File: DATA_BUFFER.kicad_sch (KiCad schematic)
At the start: 9 parts, among them IC301 ${DEVICE}

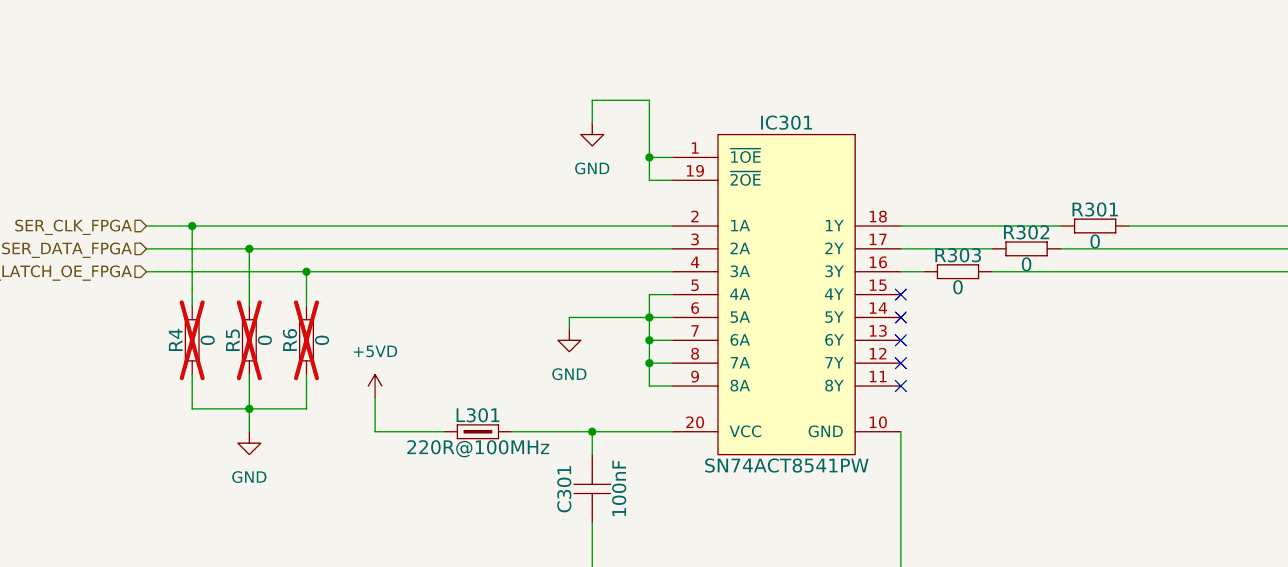
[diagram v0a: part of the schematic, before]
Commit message: Rerouted PCB Logic part
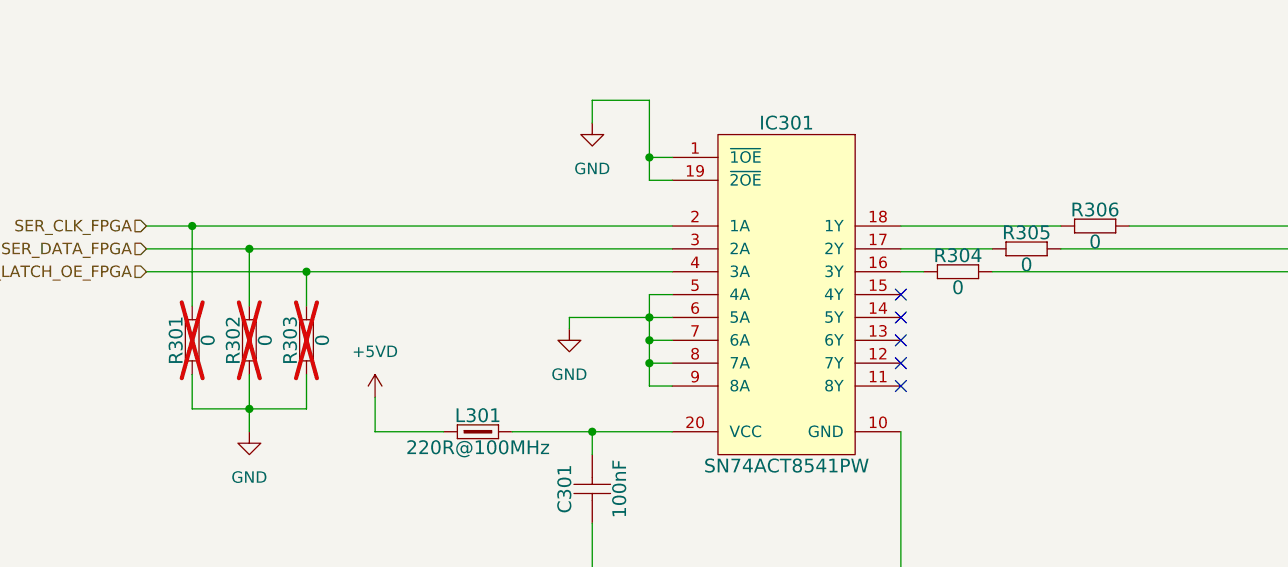
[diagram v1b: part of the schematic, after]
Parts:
- renumbered R4 to R301, R5 to R302, R6 to R303, R303 to R304, R302 to R305, R301 to R306
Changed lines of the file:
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@@
 		(dnp no)
 		(fields_autoplaced yes)
-		(property "Reference" "#PWR0304"
+		(property "Reference" "#PWR0305"
 			(at 114.3 118.11 0)
 			(effects
@@
 			(project "8CH_Analog_Front_END"
 				(path "/41597329-5145-432a-9041-5bc2cec82d9b/00694170-70ef-4ff0-8ee8-0493ce41d04f"
-					(reference "#PWR0304")
+					(reference "#PWR0305")
 					(unit 1)
 				)
@@
 		(dnp no)
 		(fields_autoplaced yes)
-		(property "Reference" "#PWR0303"
+		(property "Reference" "#PWR0302"
 			(at 90.17 92.71 0)
 			(effects
@@
 			(project "8CH_Analog_Front_END"
 				(path "/41597329-5145-432a-9041-5bc2cec82d9b/00694170-70ef-4ff0-8ee8-0493ce41d04f"
-					(reference "#PWR0303")
+					(reference "#PWR0302")
 					(unit 1)
 				)
@@
 		(on_board yes)
 		(dnp no)
-		(property "Reference" "R302"
+		(property "Reference" "R305"
 			(at 162.56 70.612 0)
 			(effects
@@
 			(project "8CH_Analog_Front_END"
 				(path "/41597329-5145-432a-9041-5bc2cec82d9b/00694170-70ef-4ff0-8ee8-0493ce41d04f"
-					(reference "R302")
+					(reference "R305")
 					(unit 1)
 				)
@@
 		(dnp no)
 		(fields_autoplaced yes)
-		(property "Reference" "#PWR0302"
+		(property "Reference" "#PWR0303"
 			(at 111.76 87.63 0)
 			(effects
@@
 			(project "8CH_Analog_Front_END"
 				(path "/41597329-5145-432a-9041-5bc2cec82d9b/00694170-70ef-4ff0-8ee8-0493ce41d04f"
-					(reference "#PWR0302")
+					(reference "#PWR0303")
 					(unit 1)
 				)
@@
 		(dnp no)
 		(fields_autoplaced yes)
-		(property "Reference" "#PWR0301"
+		(property "Reference" "#PWR0304"
 			(at 114.3 64.77 0)
 			(effects
@@
 			(project "8CH_Analog_Front_END"
 				(path "/41597329-5145-432a-9041-5bc2cec82d9b/00694170-70ef-4ff0-8ee8-0493ce41d04f"
-					(reference "#PWR0301")
+					(reference "#PWR0304")
 					(unit 1)
 				)
@@
 		(on_board yes)
 		(dnp no)
-		(property "Reference" "R303"
+		(property "Reference" "R304"
 			(at 154.94 73.152 0)
 			(effects
@@
 			(project "8CH_Analog_Front_END"
 				(path "/41597329-5145-432a-9041-5bc2cec82d9b/00694170-70ef-4ff0-8ee8-0493ce41d04f"
-					(reference "R303")
+					(reference "R304")
 					(unit 1)
 				)
@@
 		(on_board yes)
 		(dnp yes)
-		(property "Reference" "R4"
+		(property "Reference" "R301"
 			(at 68.072 82.55 0)
 			(effects
@@
 			(project "8CH_Analog_Front_END"
 				(path "/41597329-5145-432a-9041-5bc2cec82d9b/00694170-70ef-4ff0-8ee8-0493ce41d04f"
-					(reference "R4")
+					(reference "R301")
 					(unit 1)
 				)
@@
 		(on_board yes)
 		(dnp yes)
-		(property "Reference" "R6"
+		(property "Reference" "R303"
 			(at 80.772 82.55 0)
 			(effects
@@
 			(project "8CH_Analog_Front_END"
 				(path "/41597329-5145-432a-9041-5bc2cec82d9b/00694170-70ef-4ff0-8ee8-0493ce41d04f"
-					(reference "R6")
+					(reference "R303")
 					(unit 1)
 				)
@@
 		(dnp no)
 		(fields_autoplaced yes)
-		(property "Reference" "#PWR06"
+		(property "Reference" "#PWR0301"
 			(at 76.2 99.06 0)
 			(effects
@@
 			(project "8CH_Analog_Front_END"
 				(path "/41597329-5145-432a-9041-5bc2cec82d9b/00694170-70ef-4ff0-8ee8-0493ce41d04f"
-					(reference "#PWR06")
+					(reference "#PWR0301")
 					(unit 1)
 				)
@@
 		(on_board yes)
 		(dnp no)
-		(property "Reference" "R301"
+		(property "Reference" "R306"
 			(at 170.18 68.072 0)
 			(effects
@@
 			(project "8CH_Analog_Front_END"
 				(path "/41597329-5145-432a-9041-5bc2cec82d9b/00694170-70ef-4ff0-8ee8-0493ce41d04f"
-					(reference "R301")
+					(reference "R306")
 					(unit 1)
 				)
@@
 		(on_board yes)
 		(dnp yes)
-		(property "Reference" "R5"
+		(property "Reference" "R302"
 			(at 74.422 82.55 0)
 			(effects
@@
 			(project "8CH_Analog_Front_END"
 				(path "/41597329-5145-432a-9041-5bc2cec82d9b/00694170-70ef-4ff0-8ee8-0493ce41d04f"
-					(reference "R5")
+					(reference "R302")
 					(unit 1)
 				)
@@
 		(dnp no)
 		(fields_autoplaced yes)
-		(property "Reference" "#PWR0305"
+		(property "Reference" "#PWR0306"
 			(at 148.59 118.11 0)
 			(effects
@@
 			(project "8CH_Analog_Front_END"
 				(path "/41597329-5145-432a-9041-5bc2cec82d9b/00694170-70ef-4ff0-8ee8-0493ce41d04f"
-					(reference "#PWR0305")
+					(reference "#PWR0306")
 					(unit 1)
 				)

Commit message: WIP snapshot
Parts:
- removed IC301: ${DEVICE}, ICs And Semiconductors SMD:SOP65P640X120-20N, symbol CERN:Standard Logic/SN74ACT8541PW
- removed L301: 220R@100MHz, Inductors SMD:INDC1608X95N, symbol CERN:Inductors SMD/IND0603_MURATA_BLM18SG221TN1 [alt]
- removed R301, R302, R303, R304, R305, R306: 0, Resistors SMD:RESC1005X40N, symbol CERN:Resistors SMD/R0402_0R_JUMPER
- added C301, C302, C304: 100nF, Capacitors SMD:CAPC1005X55N, symbol CERN:Capacitors SMD/CC0402_100NF_25V_10%_X7R_YUDEN_TMK105B7104KVHF
- added IC301, IC302: ${DEVICE}, ICs And Semiconductors SMD:TEXAS_RHL (S-PVQFN-N24), symbol CERN_Linux:Standard Logic/SN74LVC8T245RHL
- added R301, R302, R303, R304, R306, R307, R309, R310, R311, R312, R313, R314, R315, R316, R317, R318, R319, R320, R321, R322, R323, R324, R325, R326, R327, R328: 22R6, Resistors SMD:RESC1005X40N, symbol CERN:Resistors SMD/R0402_22R6_1%_0.063W_100PPM
- added R305, R308: 220, Resistors SMD:RESC1005X40N, symbol CERN:Resistors SMD/R0402_220R_1%_0.0625W_100PPM
- renumbered C301 to C303
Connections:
- net GND: now also C301.1, C302.1, C304.1, IC301.11 (GND), IC301.12 (GND), IC301.13 (GND), IC301.22 (~{OE}), IC302.11 (GND), IC302.12 (GND), IC302.13 (GND), IC302.22 (~{OE}), R305.1, R308.1
- net SER_CLK_FPGA: now also R302.1
- net +3V3D: now reaches C303.2
- net +3V3D: now also C301.2, C302.2, C304.2, IC301.1 (VCCA), IC301.2 (DIR), IC301.23 (VCCB), IC301.24 (VCCB), IC302.1 (VCCA), IC302.2 (DIR), IC302.23 (VCCB), IC302.24 (VCCB)
- new net: IC302.10 (A8), IC302.7 (A5), IC302.8 (A6), IC302.9 (A7), R302.2, R305.2
- new net: IC301.9 (A7), R307.2
- new net: IC301.8 (A6), R311.2
- new net: IC301.3 (A1), R303.2
- new net: IC301.20 (B2), R313.1
- new net: IC301.21 (B1), R321.1
- new net: IC302.21 (B1), R325.1
- new net: IC301.14 (B8), R316.1
- new net: IC302.3 (A1), IC302.4 (A2), IC302.5 (A3), IC302.6 (A4), R301.2, R308.2
- new net: IC301.17 (B5), R323.1
- new net: IC302.16 (B6), R319.1
- new net: IC301.5 (A3), R306.2
- new net: IC301.18 (B4), R314.1
- new net: IC302.14 (B8), R320.1
- new net: IC302.15 (B7), R328.1
- new net: IC302.17 (B5), R327.1
- new net: IC302.18 (B4), R318.1
- new net: IC302.19 (B3), R326.1
- new net: IC302.20 (B2), R317.1
- new net: IC301.10 (A8), R312.2
- new net: IC301.6 (A4), R310.2
- new net: IC301.19 (B3), R322.1
- new net: IC301.4 (A2), R309.2
- new net: IC301.15 (B7), R324.1
- new net: IC301.16 (B6), R315.1
- new net: IC301.7 (A5), R304.2
- new net SER_CLK_CH0: R327.2
- new net SER_CLK_CH1: R319.2
- new net SER_CLK_CH2: R328.2
- new net SER_CLK_CH3: R320.2
- new net SER_DATA0: R321.2
- new net SER_DATA1: R313.2
- new net SER_DATA2: R322.2
- new net SER_DATA3: R314.2
- new net SER_DATA4: R323.2
- new net SER_DATA5: R315.2
- new net SER_DATA6: R324.2
- new net SER_DATA7: R316.2
- new net SER_DATA_FPGA0: R303.1
- new net SER_DATA_FPGA1: R309.1
- new net SER_DATA_FPGA2: R306.1
- new net SER_DATA_FPGA3: R310.1
- new net SER_DATA_FPGA4: R304.1
- new net SER_DATA_FPGA5: R311.1
- new net SER_DATA_FPGA6: R307.1
- new net SER_DATA_FPGA7: R312.1
- new net SER_RCLK_CH0: R325.2
- new net SER_RCLK_CH1: R317.2
- new net SER_RCLK_CH2: R326.2
- new net SER_RCLK_CH3: R318.2
- new net SER_RCLK_FPGA: R301.1
- no-connect marks 5 -> 0
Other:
- note added: "Place series resistors close to IC6."
- note added: "Place series resistors close to KR SoM connector."
- note added: "Shiftreg DATA buffer. - DIR=1 (A->B), powered from Vcca (3.3V) - Each SER_DATA line handles a chain of 3x8-bit SRs (24-bits in total) - The above gives 16ns x 24 = 500ns update time (62.5 MHz CLK, abort gap is 3us) - Two SER_DATA lines go to a single AFE block (one for channel A, one for channel B)"
- note added: "Shiftreg clocks buffer. - DIR=1 (A->B), powered from Vcca (3.3V) - Acts as a clock fanout to avoid excessive load on the clock lines (1 dedicated shiftreg clock per plane)."
- note removed: "DATA"
- moved on the sheet: C303

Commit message: Update project files and backups
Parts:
- added R329, R330, R331, R332, R333, R334, R335, R336: 220, Resistors SMD:RESC1005X40N, symbol CERN:Resistors SMD/R0402_220R_1%_0.0625W_100PPM
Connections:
- net GND: now also R329.1, R330.1, R331.1, R332.1, R333.1, R334.1, R335.1, R336.1
- net SER_CLK_CH0: now also R336.2
- net SER_CLK_CH1: now also R330.2
- net SER_CLK_CH2: now also R332.2
- net SER_CLK_CH3: now also R334.2
- net SER_RCLK_CH0: now also R335.2
- net SER_RCLK_CH1: now also R329.2
- net SER_RCLK_CH2: now also R331.2
- net SER_RCLK_CH3: now also R333.2
- net at R307.2: now also IC301.4 (A2); no longer IC301.9 (A7)
- net at R311.2: now also IC301.5 (A3); no longer IC301.8 (A6)
- net at R303.2: now also IC301.10 (A8); no longer IC301.3 (A1)
- net at R313.1: now also IC301.15 (B7); no longer IC301.20 (B2)
- net at R321.1: now also IC301.14 (B8); no longer IC301.21 (B1)
- net at R325.1: now also IC302.18 (B4); no longer IC302.21 (B1)
- net at R316.1: now also IC301.21 (B1); no longer IC301.14 (B8)
- net at R323.1: now also IC301.18 (B4); no longer IC301.17 (B5)
- net at R319.1: now also IC302.15 (B7); no longer IC302.16 (B6)
- net at R306.2: now also IC301.8 (A6); no longer IC301.5 (A3)
- net at R314.1: now also IC301.17 (B5); no longer IC301.18 (B4)
- net at IC302.14 (B8): now also R327.1; no longer R320.1
- net at R328.1: now also IC302.16 (B6); no longer IC302.15 (B7)
- net at IC302.17 (B5): now also R320.1; no longer R327.1
- net at R318.1: now also IC302.21 (B1); no longer IC302.18 (B4)
- net at IC302.19 (B3): now also R317.1; no longer R326.1
- net at IC302.20 (B2): now also R326.1; no longer R317.1
- net at R312.2: now also IC301.3 (A1); no longer IC301.10 (A8)
- net at R310.2: now also IC301.7 (A5); no longer IC301.6 (A4)
- net at R322.1: now also IC301.16 (B6); no longer IC301.19 (B3)
- net at R309.2: now also IC301.9 (A7); no longer IC301.4 (A2)
- net at R324.1: now also IC301.20 (B2); no longer IC301.15 (B7)
- net at R315.1: now also IC301.19 (B3); no longer IC301.16 (B6)
- net at R304.2: now also IC301.6 (A4); no longer IC301.7 (A5)
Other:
- note added: "Flipped for easier routing"
- note added: "Optional parallel termination resistors for shifreg clock lines. Left just in case we had excessive ringing :-) PLACE AT THE END OF CLOCK CHAIN!"
- moved on the sheet: R303, R304, R306, R307, R309, R310, R311, R312, R313, R314, R315, R316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
